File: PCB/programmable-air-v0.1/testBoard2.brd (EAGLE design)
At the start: 28.1 x 28.1 mm, 1 part

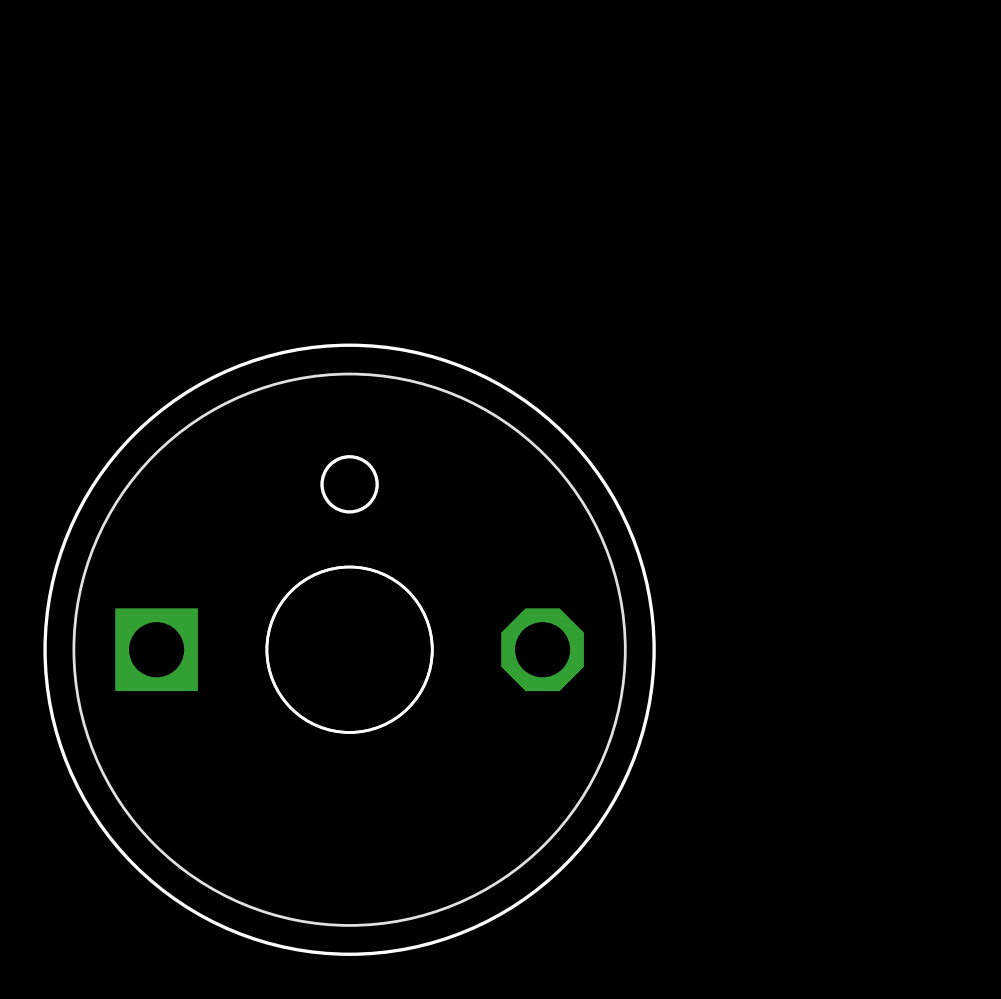
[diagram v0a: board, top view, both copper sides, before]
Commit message: Made pump nad valve PCB library. PCB Mockup made. Added arduino nano footprint.
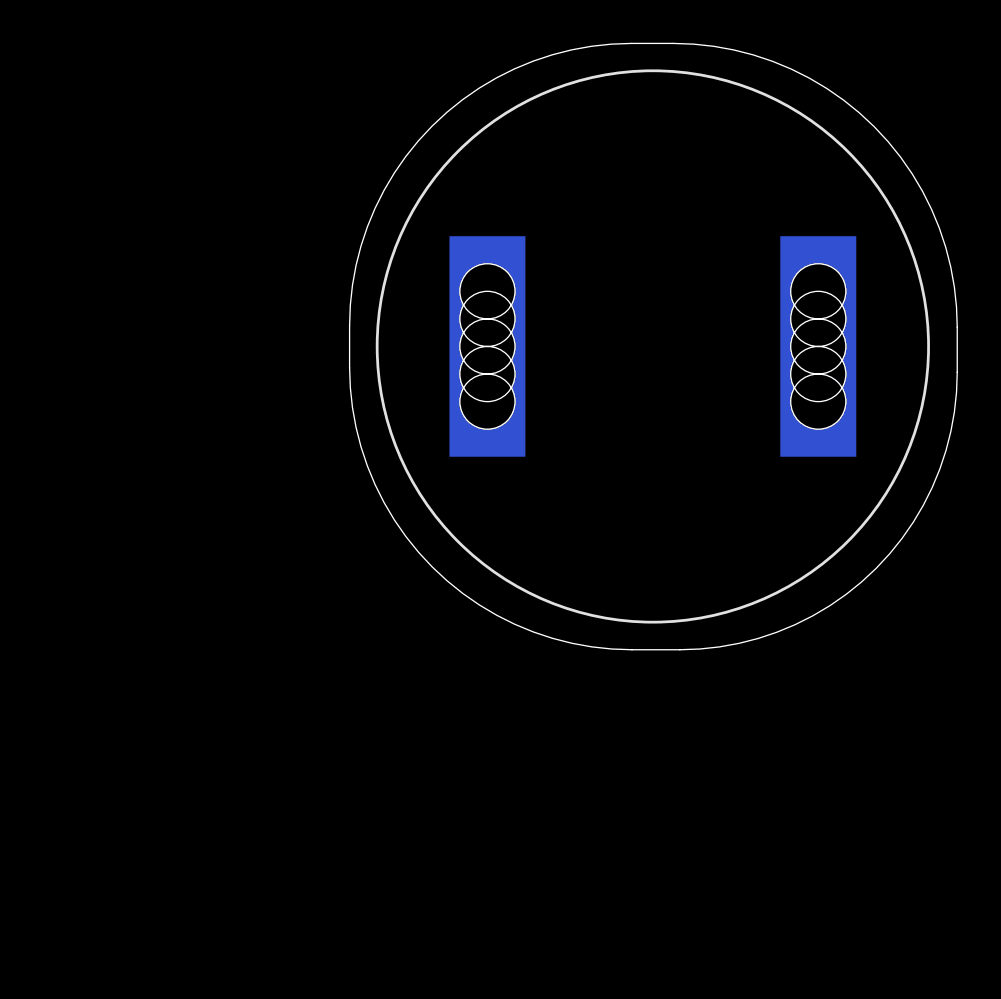
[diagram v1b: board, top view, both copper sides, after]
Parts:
- removed E$1: (no value), programmable-air-components:A5F083
- added U$1: CJV23-SOLENOID-VALVE, programmable-air-components:CJV23
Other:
- board size 28.1 x 28.1 mm -> 28 x 27.9 mm
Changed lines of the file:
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@@
 <settings>
 <setting alwaysvectorfont="no"/>
-<setting keepoldvectorfont="yes"/>
 <setting verticaltext="up"/>
 </settings>
@@
 <layers>
 <layer number="1" name="Top" color="4" fill="1" visible="yes" active="yes"/>
-<layer number="2" name="Route2" color="1" fill="3" visible="no" active="no"/>
-<layer number="3" name="Route3" color="4" fill="3" visible="no" active="no"/>
-<layer number="4" name="Route4" color="1" fill="4" visible="no" active="no"/>
-<layer number="5" name="Route5" color="4" fill="4" visible="no" active="no"/>
-<layer number="6" name="Route6" color="1" fill="8" visible="no" active="no"/>
-<layer number="7" name="Route7" color="4" fill="8" visible="no" active="no"/>
-<layer number="8" name="Route8" color="1" fill="2" visible="no" active="no"/>
-<layer number="9" name="Route9" color="4" fill="2" visible="no" active="no"/>
-<layer number="10" name="Route10" color="1" fill="7" visible="no" active="no"/>
-<layer number="11" name="Route11" color="4" fill="7" visible="no" active="no"/>
-<layer number="12" name="Route12" color="1" fill="5" visible="no" active="no"/>
-<layer number="13" name="Route13" color="4" fill="5" visible="no" active="no"/>
-<layer number="14" name="Route14" color="1" fill="6" visible="no" active="no"/>
-<layer number="15" name="Route15" color="4" fill="6" visible="no" active="no"/>
 <layer number="16" name="Bottom" color="1" fill="1" visible="yes" active="yes"/>
 <layer number="17" name="Pads" color="2" fill="1" visible="yes" active="yes"/>
 <layer number="18" name="Vias" color="2" fill="1" visible="yes" active="yes"/>
 <layer number="19" name="Unrouted" color="6" fill="1" visible="yes" active="yes"/>
-<layer number="20" name="Dimension" color="15" fill="1" visible="yes" active="yes"/>
+<layer number="20" name="Dimension" color="24" fill="1" visible="yes" active="yes"/>
 <layer number="21" name="tPlace" color="7" fill="1" visible="yes" active="yes"/>
 <layer number="22" name="bPlace" color="7" fill="1" visible="yes" active="yes"/>
@@
 <layer number="43" name="vRestrict" color="2" fill="10" visible="yes" active="yes"/>
 <layer number="44" name="Drills" color="7" fill="1" visible="no" active="yes"/>
-<layer number="45" name="Holes" color="7" fill="1" visible="yes" active="yes"/>
+<layer number="45" name="Holes" color="7" fill="1" visible="no" active="yes"/>
 <layer number="46" name="Milling" color="3" fill="1" visible="no" active="yes"/>
 <layer number="47" name="Measures" color="7" fill="1" visible="no" active="yes"/>
@@
 <layer number="51" name="tDocu" color="7" fill="1" visible="yes" active="yes"/>
 <layer number="52" name="bDocu" color="7" fill="1" visible="yes" active="yes"/>
+<layer number="88" name="SimResults" color="9" fill="1" visible="no" active="no"/>
+<layer number="89" name="SimProbes" color="9" fill="1" visible="no" active="no"/>
 <layer number="90" name="Modules" color="5" fill="1" visible="no" active="no"/>
 <layer number="91" name="Nets" color="2" fill="1" visible="no" active="no"/>
@@
 <board>
 <plain>
-<circle x="0" y="0" radius="14.02760625" width="0.1524" layer="20"/>
-<hole x="0" y="0" drill="7.62"/>
-<circle x="0" y="7.62" radius="1.27" width="0.1524" layer="20"/>
+<wire x1="0" y1="14.938928125" x2="0" y2="13.00816875" width="0" layer="20"/>
+<wire x1="0" y1="13.00816875" x2="13.00816875" y2="0" width="0" layer="20" curve="90"/>
+<wire x1="13.00816875" y1="0" x2="15.214578125" y2="0" width="0" layer="20"/>
+<wire x1="15.214578125" y1="0" x2="27.991" y2="12.776421875" width="0" layer="20" curve="90"/>
+<wire x1="27.991" y1="12.776421875" x2="27.991" y2="14.85203125" width="0" layer="20"/>
+<wire x1="27.991" y1="14.85203125" x2="14.91303125" y2="27.93" width="0" layer="20" curve="90"/>
+<wire x1="14.91303125" y1="27.93" x2="12.991071875" y2="27.93" width="0" layer="20"/>
+<wire x1="12.991071875" y1="27.93" x2="0" y2="14.938928125" width="0" layer="20" curve="90"/>
 </plain>
 <attributes>
@@
 </autorouter>
 <elements>
-<element name="E$1" library="programmable-air-components" package="A5F083" value="" x="0" y="0"/>
+<element name="U$1" library="programmable-air-components" package="CJV23" value="CJV23-SOLENOID-VALVE" x="13.97" y="13.97"/>
 </elements>
 <signals>
